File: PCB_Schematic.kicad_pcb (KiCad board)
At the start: 2 copper layers, 78.9 x 94.7 mm, 111 parts, among them J2 Programming Header, J3 SDOAG_Connector, J4 Power_Connector, J5 Ultrasonic, J6 USB_A, J7 IMU_1, J8 IMU_2, Q1 BSS138, SW1 Reset Switch, U1 STM32F091RCTx, U2 FT232RL, U3 LM1117MP-ADJ, U4 TPS54331QDRQ1, U5 MAX7375AXR805

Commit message: hi
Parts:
- moved H2 1.74 mm to (163.7, 36.1)
- moved H1 1.05 mm to (91.4, 36.1)
- moved H4 1.05 mm to (163.3, 124.0)
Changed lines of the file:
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@@
 	(footprint "MountingHole:MountingHole_2.2mm_M2"
 		(layer "F.Cu")
-		(at 91.694 37.084)
+		(at 91.44 36.068)
 		(descr "Mounting Hole 2.2mm, no annular, M2")
 		(tags "mounting hole 2.2mm no annular m2")
@@
 	(footprint "MountingHole:MountingHole_2.2mm_M2"
 		(layer "F.Cu")
-		(at 163.068 122.936)
+		(at 163.322 123.952)
 		(descr "Mounting Hole 2.2mm, no annular, M2")
 		(tags "mounting hole 2.2mm no annular m2")
@@
 	(footprint "MountingHole:MountingHole_2.2mm_M2"
 		(layer "F.Cu")
-		(at 162.56 37.338)
+		(at 163.749 36.068)
 		(descr "Mounting Hole 2.2mm, no annular, M2")
 		(tags "mounting hole 2.2mm no annular m2")

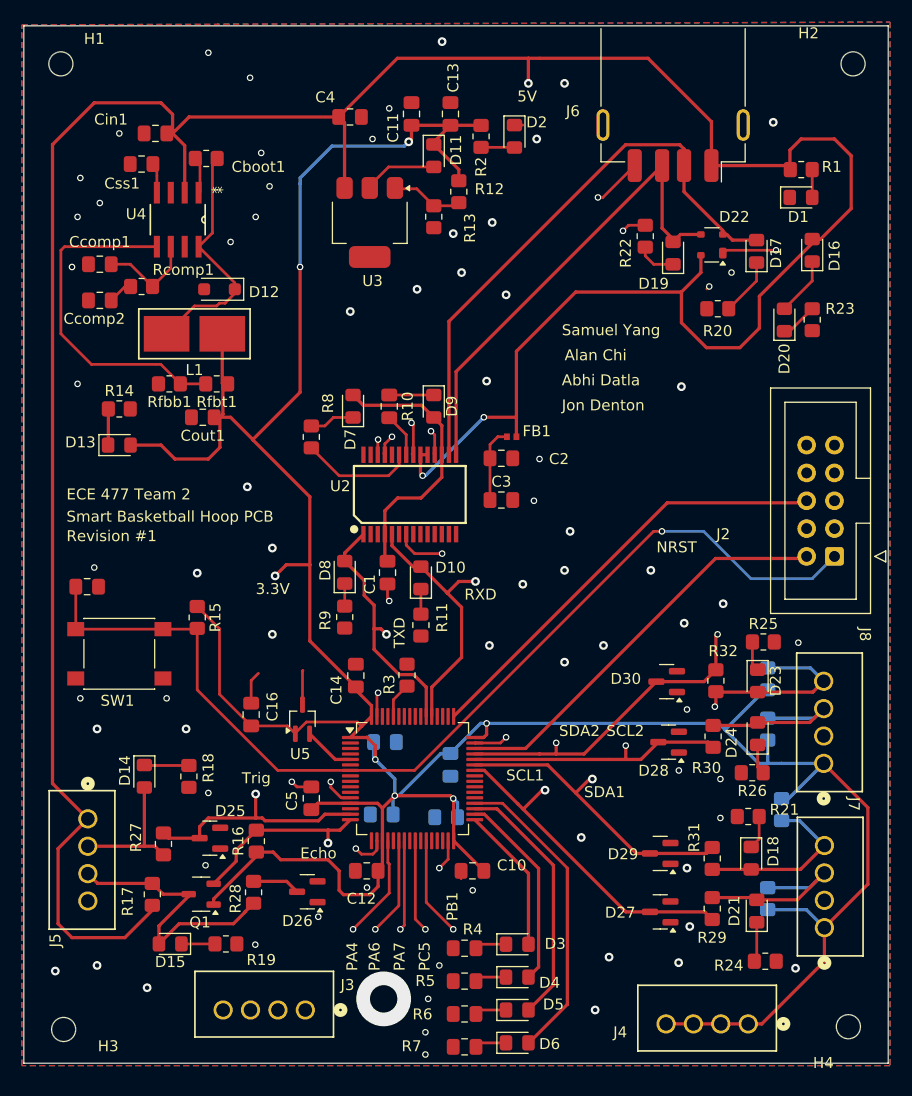
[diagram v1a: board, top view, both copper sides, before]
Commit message: mounting holes locations
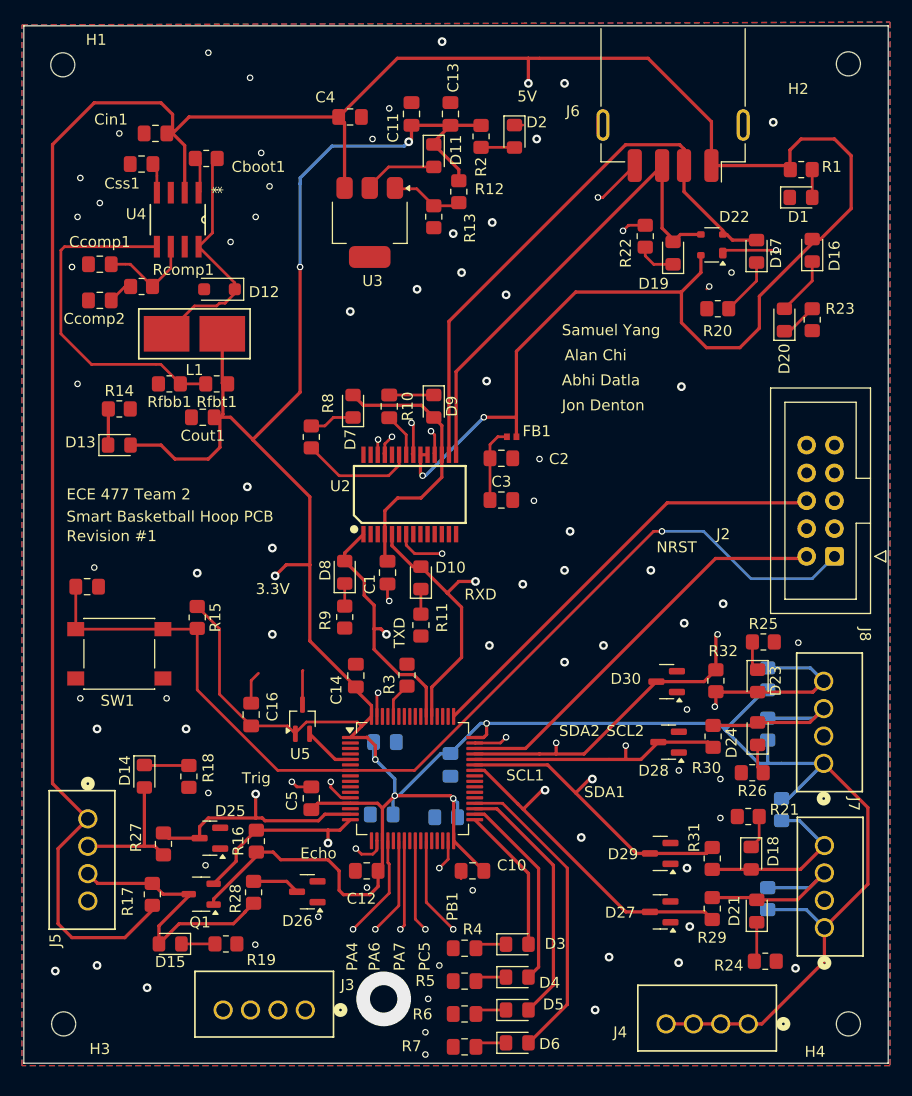
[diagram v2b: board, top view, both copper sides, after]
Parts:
- moved H3 0.51 mm to (91.7, 123.7)
- moved H2 0.43 mm to (163.3, 36.1)
- moved H4 0.25 mm to (163.3, 123.7)
- moved H1 0.19 mm to (91.6, 36.2)
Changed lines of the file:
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@@
 	(footprint "MountingHole:MountingHole_2.2mm_M2"
 		(layer "F.Cu")
-		(at 91.44 36.068)
+		(at 91.613 36.156)
 		(descr "Mounting Hole 2.2mm, no annular, M2")
 		(tags "mounting hole 2.2mm no annular m2")
@@
 	(footprint "MountingHole:MountingHole_2.2mm_M2"
 		(layer "F.Cu")
-		(at 163.322 123.952)
+		(at 163.322 123.698)
 		(descr "Mounting Hole 2.2mm, no annular, M2")
 		(tags "mounting hole 2.2mm no annular m2")
 		(property "Reference" "H4"
-			(at -2.286 3.302 0)
+			(at -3.048 2.54 0)
 			(layer "F.SilkS")
 			(effects
@@
 		)
 		(property "Value" "MountingHole"
-			(at -2.129 -3.744 0)
+			(at -1.524 -3.302 0)
 			(layer "F.Fab")
 			(effects
@@
 	(footprint "MountingHole:MountingHole_2.2mm_M2"
 		(layer "F.Cu")
-		(at 163.749 36.068)
+		(at 163.322 36.068)
 		(descr "Mounting Hole 2.2mm, no annular, M2")
 		(tags "mounting hole 2.2mm no annular m2")
 		(property "Reference" "H2"
-			(at -4.064 -2.794 180)
+			(at -4.572 2.286 180)
 			(layer "F.SilkS")
 			(effects
@@
 		)
 		(property "Value" "MountingHole"
-			(at -7.971 -0.95 0)
+			(at -2.286 3.556 0)
 			(layer "F.Fab")
 			(effects
@@
 	(footprint "MountingHole:MountingHole_2.2mm_M2"
 		(layer "F.Cu")
-		(at 91.694 124.206)
+		(at 91.694 123.698)
 		(descr "Mounting Hole 2.2mm, no annular, M2")
 		(tags "mounting hole 2.2mm no annular m2")
 		(property "Reference" "H3"
-			(at 4.064 1.524 0)
+			(at 3.302 2.286 0)
 			(layer "F.SilkS")
 			(effects

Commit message: updated fp
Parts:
- added D11: BAT60JFILM, Diode_SMD:D_SOD-323_HandSoldering, F.Cu at (125.7, 53.6)
- D12: footprint Diode_SMD:D_SOD-123F -> Diode_SMD:D_SOD-123
- D16: footprint Diode_SMD:D_0805_2012Metric_Pad1.15x1.40mm_HandSolder -> Diode_SMD:D_SOD-323_HandSoldering
- D22: footprint Package_TO_SOT_SMD:SOT-143 -> Library:PRT
- moved D12 12.5 mm to (109.7, 44.7), turned to 0 degrees
- moved D16 0.25 mm to (160.0, 53.3)
- turned D22 to 90 degrees
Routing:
- net +3.3V: track 301.1 -> 310.2 mm
- net Net-(D11-A): track 6.83 -> 15.1 mm
- net GND: track 53.6 -> 57.0 mm
- net Net-(D12-K): track 22.0 -> 24.3 mm

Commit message: BOM done
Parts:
- SW1: footprint Button_Switch_SMD:SW_SPST_PTS645 -> Library:SW_TS04-66-55-BK-160-SMT
- moved J2 0.36 mm to (161.8, 81.3)
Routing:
- net GND: track 57.0 -> 59.8 mm, vias 89 -> 91
- net /NRST: track 93.5 -> 91.2 mm
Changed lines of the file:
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@@
 	(footprint "Connector_IDC:IDC-Header_2x05_P2.54mm_Vertical"
 		(layer "F.Cu")
-		(at 162.052 81.026 180)
+		(at 161.798 81.28 180)
 		(descr "Through hole IDC box header, 2x05, 2.54mm pitch, DIN 41651 / IEC 60603-13, double rows, https://docs.google.com/spreadsheets/d/16SsEcesNF15N3Lb4niX7dcUr-NY5_MFPQhobNuNppn4/edit#gid=0")
 		(tags "Through hole vertical IDC box header THT 2x05 2.54mm double row")
 		(property "Reference" "J2"
-			(at 10.16 2.032 0)
+			(at 1.27 -6.1 360)
 			(layer "F.SilkS")
 			(effects
@@
 		)
 		(property "Value" "Programming Header"
-			(at 3.302 16.51 0)
+			(at 1.27 16.26 360)
 			(layer "F.Fab")
 			(effects
@@
 		)
 		(fp_text user "${REFERENCE}"
-			(at 10.16 13.212 90)
+			(at 1.27 5.08 90)
 			(layer "F.Fab")
 			(effects
@@
 		)
 	)
-	(footprint "Button_Switch_SMD:SW_SPST_PTS645"
+	(footprint "Library:SW_TS04-66-55-BK-160-SMT"
 		(layer "F.Cu")
 		(at 96.774 89.916 180)
-		(descr "C&K Components SPST SMD PTS645 Series 6mm Tact Switch")
-		(tags "SPST Button Switch")
 		(property "Reference" "SW1"
-			(at 0.17 -4.282 0)
+			(at -0.508 -4.318 180)
 			(layer "F.SilkS")
 			(effects
@@
 		)
 		(property "Value" "Reset Switch"
-			(at 0 4.15 0)
+			(at 10.922 3.81 180)
 			(layer "F.Fab")
 			(effects
@@
 			)
 		)
-		(property "Footprint" "Button_Switch_SMD:SW_SPST_PTS645"
+		(property "Footprint" "Library:SW_TS04-66-55-BK-160-SMT"
 			(at 0 0 180)
-			(unlocked yes)
 			(layer "F.Fab")
 			(hide yes)
@@
 		(property "Datasheet" ""
 			(at 0 0 180)
-			(unlocked yes)
 			(layer "F.Fab")
 			(hide yes)
@@
 		(property "Description" "Push button switch, generic, two pins"
 			(at 0 0 180)
-			(unlocked yes)
 			(layer "F.Fab")
 			(hide yes)
@@
 		(attr smd)
 		(fp_line
-			(start 3.23 3.23)
-			(end 3.23 3.2)
-			(stroke
-				(width 0.12)
-				(type solid)
-			)
-			(layer "F.SilkS")
-		)
-		(fp_line
-			(start 3.23 -1.3)
-			(end 3.23 1.3)
-			(stroke
-				(width 0.12)
-				(type solid)
-			)
-			(layer "F.SilkS")
-		)
-		(fp_line
-			(start 3.23 -3.23)
-			(end 3.23 -3.2)
-			(stroke
-				(width 0.12)
-				(type solid)
-			)
-			(layer "F.SilkS")
-		)
-		(fp_line
-			(start -3.23 3.23)
-			(end 3.23 3.23)
+			(start 3 3)
+			(end 3 -3)
 			(stroke
-				(width 0.12)
+				(width 0.127)
 				(type solid)
 			)
@@
 		)
 		(fp_line
-			(start -3.23 3.23)
-			(end -3.23 3.2)
+			(start 3 -3)
+			(end -3 -3)
 			(stroke
-				(width 0.12)
+				(width 0.127)
 				(type solid)
 			)
@@
 		)
 		(fp_line
-			(start -3.23 -1.3)
-			(end -3.23 1.3)
+			(start -3 3)
+			(end 3 3)
 			(stroke
-				(width 0.12)
+				(width 0.127)
 				(type solid)
 			)
@@
 		)
 		(fp_line
-			(start -3.23 -3.2)
-			(end -3.23 -3.23)
+			(start -3 -3)
+			(end -3 3)
 			(stroke
-				(width 0.12)
+				(width 0.127)
 				(type solid)
 			)
 			(layer "F.SilkS")
 		)
-		(fp_line
-			(start -3.23 -3.23)
-			(end 3.23 -3.23)
+		(fp_circle
+			(center -6.25 -2.25)
+			(end -6.15 -2.25)
 			(stroke
-				(width 0.12)
+				(width 0.2)
 				(type solid)
 			)
+			(fill none)
 			(layer "F.SilkS")
 		)
 		(fp_line
-			(start 5.05 3.4)
-			(end 5.05 -3.4)
+			(start 5.85 3.25)
+			(end 5.85 -3.25)
 			(stroke
 				(width 0.05)
@@
 		)
 		(fp_line
-			(start -5.05 3.4)
-			(end 5.05 3.4)
+			(start 5.85 -3.25)
+			(end -5.85 -3.25)
 			(stroke
 				(width 0.05)
@@
 		)
 		(fp_line
-			(start -5.05 -3.4)
-			(end 5.05 -3.4)
+			(start -5.85 3.25)
+			(end 5.85 3.25)
 			(stroke
 				(width 0.05)
@@
 		)
 		(fp_line
-			(start -5.05 -3.4)
-			(end -5.05 3.4)
+			(start -5.85 -3.25)
+			(end -5.85 3.25)
 			(stroke
 				(width 0.05)
@@
 			(end 3 -3)
 			(stroke
-				(width 0.1)
+				(width 0.127)
 				(type solid)
 			)
@@
 			(end -3 -3)
 			(stroke
-				(width 0.1)
+				(width 0.127)
 				(type solid)
 			)
@@
 			(end 3 3)
 			(stroke
-				(width 0.1)
+				(width 0.127)
 				(type solid)
 			)
@@
 			(end -3 3)
 			(stroke
-				(width 0.1)
+				(width 0.127)
 				(type solid)
 			)
@@
 		)
 		(fp_circle
-			(center 0 0)
-			(end 1.75 -0.05)
+			(center -6.25 -2.25)
+			(end -6.15 -2.25)
 			(stroke
-				(width 0.1)
+				(width 0.2)
 				(type solid)
 			)
@@
 			(layer "F.Fab")
 		)
-		(fp_text user "${REFERENCE}"
-			(at 0.17 -4.282 0)
-			(layer "F.Fab")
-			(effects
-				(font
-					(size 1 1)
-					(thickness 0.15)
-				)
-			)
-		)
-		(pad "1" smd rect
-			(at -3.98 -2.25 180)
-			(size 1.55 1.3)
-			(layers "F.Cu" "F.Paste" "F.Mask")
-			(net 1 "GND")
-			(pinfunction "1")
-			(pintype "passive")
-		)
 		(pad "1" smd rect
-			(at 3.98 -2.25 180)
-			(size 1.55 1.3)
+			(at -4.55 -2.25 180)
+			(size 2.1 1.4)
 			(layers "F.Cu" "F.Paste" "F.Mask")
 			(net 1 "GND")
 			(pinfunction "1")
 			(pintype "passive")
+			(solder_mask_margin 0.102)
 		)
 		(pad "2" smd rect
-			(at -3.98 2.25 180)
-			(size 1.55 1.3)
+			(at -4.55 2.25 180)
+			(size 2.1 1.4)
 			(layers "F.Cu" "F.Paste" "F.Mask")
 			(net 5 "/NRST")
 			(pinfunction "2")
 			(pintype "passive")
+			(solder_mask_margin 0.102)
 		)
-		(pad "2" smd rect
-			(at 3.98 2.25 180)
-			(size 1.55 1.3)
+		(pad "3" smd rect
+			(at 4.55 -2.25 180)
+			(size 2.1 1.4)
 			(layers "F.Cu" "F.Paste" "F.Mask")
-			(net 5 "/NRST")
-			(pinfunction "2")
-			(pintype "passive")
+			(solder_mask_margin 0.102)
 		)
-		(model "${KICAD8_3DMODEL_DIR}/Button_Switch_SMD.3dshapes/SW_SPST_PTS645.wrl"
-			(offset
-				(xyz 0 0 0)
-			)
-			(scale
-				(xyz 1 1 1)
-			)
-			(rotate
-				(xyz 0 0 0)
-			)
+		(pad "4" smd rect
+			(at 4.55 2.25 180)
+			(size 2.1 1.4)
+			(layers "F.Cu" "F.Paste" "F.Mask")
+			(solder_mask_margin 0.102)
 		)
 	)
@@
 	)
 	(segment
+		(start 101.324 94.256)
+		(end 100.838 94.742)
+		(width 0.254)
+		(layer "F.Cu")
+		(net 1)
+	)
+	(segment
 		(start 126.791 108.667)
 		(end 125.984 109.474)
@@
 	)
 	(segment
+		(start 101.324 92.166)
+		(end 101.324 94.256)
+		(width 0.254)
+		(layer "F.Cu")
+		(net 1)
+	)
+	(segment
 		(start 129.272 98.058)
 		(end 129.286 98.044)
@@
 	)
 	(via
+		(at 100.838 94.742)
+		(size 0.6)
+		(drill 0.381)
+		(layers "F.Cu" "B.Cu")
+		(net 1)
+	)
+	(via
 		(at 104.902 102.616)
 		(size 0.6)
@@
 	)
 	(via
+		(at 113.538 91.44)
+		(size 0.6)
+		(drill 0.381)
+		(layers "F.Cu" "B.Cu")
+		(net 1)
+	)
+	(via
 		(at 110.744 88.138)
 		(size 0.8)
@@
 	)
 	(via
-		(at 101.092 93.98)
+		(at 109.474 91.694)
 		(size 0.6)
 		(drill 0.381)
@@
 	)
 	(via
-		(at 93.218 93.98)
+		(at 97.028 95.758)
 		(size 0.6)
 		(drill 0.381)
@@
 	)
 	(segment
-		(start 92.801 87.659)
-		(end 92.794 87.666)
-		(width 0.25)
+		(start 96.678 87.666)
+		(end 101.324 87.666)
+		(width 0.254)
 		(layer "F.Cu")
 		(net 5)
@@
 	)
 	(segment
-		(start 103.818 87.666)
-		(end 103.886 87.598)
-		(width 0.25)
+		(start 92.801 83.789)
+		(end 96.678 87.666)
+		(width 0.254)
 		(layer "F.Cu")
 		(net 5)
 	)
 	(segment
-		(start 92.801 83.789)
-		(end 92.801 87.659)
+		(start 103.818 87.666)
+		(end 103.886 87.598)
 		(width 0.254)
 		(layer "F.Cu")
@@
 	)
 	(segment
-		(start 92.794 87.666)
-		(end 100.754 87.666)
-		(width 0.254)
-		(layer "F.Cu")
-		(net 5)
-	)
-	(segment
 		(start 123.724 100.558)
 		(end 117.866 100.558)
@@
 	)
 	(segment
-		(start 100.754 87.666)
+		(start 101.324 87.666)
 		(end 103.818 87.666)
 		(width 0.254)

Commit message: footprint verf
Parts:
- D11: footprint Diode_SMD:D_0805_2012Metric_Pad1.15x1.40mm_HandSolder -> Diode_SMD:D_SOD-323_HandSoldering
- moved D11 0.55 mm to (125.2, 44.9)
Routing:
- net +3.3V: track 310.2 -> 310.8 mm
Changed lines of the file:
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@@
 		(tags "Through hole vertical IDC box header THT 2x05 2.54mm double row")
 		(property "Reference" "J2"
-			(at 1.27 -6.1 360)
+			(at 1.27 -6.1 0)
 			(layer "F.SilkS")
 			(effects
@@
 		)
 		(property "Value" "Programming Header"
-			(at 1.27 16.26 360)
+			(at 1.27 16.26 0)
 			(layer "F.Fab")
 			(effects
@@
 		)
 		(property "Value" "Reset Switch"
-			(at 10.922 3.81 180)
+			(at -0.508 0.762 180)
 			(layer "F.Fab")
 			(effects
@@
 		)
 	)
-	(footprint "Diode_SMD:D_0805_2012Metric_Pad1.15x1.40mm_HandSolder"
+	(footprint "Diode_SMD:D_SOD-323_HandSoldering"
 		(layer "F.Cu")
-		(at 125.476 44.45 -90)
-		(descr "Diode SMD 0805 (2012 Metric), square (rectangular) end terminal, IPC_7351 nominal, (Body size source: https://docs.google.com/spreadsheets/d/1BsfQQcO9C6DZCsRaXUlFlo91Tg2WpOkGARC1WS5S8t0/edit?usp=sharing), generated with kicad-footprint-generator")
-		(tags "diode handsolder")
+		(at 125.222 44.938 -90)
+		(descr "SOD-323")
+		(tags "SOD-323")
 		(property "Reference" "D11"
-			(at -0.508 -2.032 90)
+			(at -0.742 -2.286 -90)
 			(layer "F.SilkS")
 			(effects
@@
 		)
 		(property "Value" "BAT60JFILM"
-			(at 2 1.142 90)
+			(at 0.1 1.9 -90)
 			(layer "F.Fab")
 			(effects
@@
 			)
 		)
-		(property "Footprint" "Diode_SMD:D_0805_2012Metric_Pad1.15x1.40mm_HandSolder"
+		(property "Footprint" "Diode_SMD:D_SOD-323_HandSoldering"
 			(at 0 0 -90)
 			(unlocked yes)
@@
 		(attr smd)
 		(fp_line
-			(start -1.86 0.96)
-			(end 1 0.96)
+			(start -2.01 0.85)
+			(end 1.25 0.85)
 			(stroke
 				(width 0.12)
@@
 		)
 		(fp_line
-			(start -1.86 -0.96)
-			(end -1.86 0.96)
+			(start -2.01 -0.85)
+			(end -2.01 0.85)
 			(stroke
 				(width 0.12)
@@
 		)
 		(fp_line
-			(start 1 -0.96)
-			(end -1.86 -0.96)
+			(start -2.01 -0.85)
+			(end 1.25 -0.85)
 			(stroke
 				(width 0.12)
@@
 		)
 		(fp_line
-			(start -1.85 0.95)
-			(end -1.85 -0.95)
+			(start -2 0.95)
+			(end 2 0.95)
 			(stroke
 				(width 0.05)
@@
 		)
 		(fp_line
-			(start 1.85 0.95)
-			(end -1.85 0.95)
+			(start -2 -0.95)
+			(end -2 0.95)
 			(stroke
 				(width 0.05)
@@
 		)
 		(fp_line
-			(start -1.85 -0.95)
-			(end 1.85 -0.95)
+			(start -2 -0.95)
+			(end 2 -0.95)
 			(stroke
 				(width 0.05)
@@
 		)
 		(fp_line
-			(start 1.85 -0.95)
-			(end 1.85 0.95)
+			(start 2 -0.95)
+			(end 2 0.95)
 			(stroke
 				(width 0.05)
@@
 		)
 		(fp_line
-			(start -1 0.6)
-			(end 1 0.6)
+			(start -0.9 0.7)
+			(end -0.9 -0.7)
 			(stroke
 				(width 0.1)
@@
 		)
 		(fp_line
-			(start 1 0.6)
-			(end 1 -0.6)
+			(start 0.9 0.7)
+			(end -0.9 0.7)
 			(stroke
 				(width 0.1)
@@
 		)
 		(fp_line
-			(start -1 -0.3)
-			(end -1 0.6)
+			(start 0.2 0.35)
+			(end -0.3 0)
 			(stroke
 				(width 0.1)
@@
 		)
 		(fp_line
-			(start -0.7 -0.6)
-			(end -1 -0.3)
+			(start -0.3 0)
+			(end -0.5 0)
 			(stroke
 				(width 0.1)
@@
 		)
 		(fp_line
-			(start 1 -0.6)
-			(end -0.7 -0.6)
+			(start -0.3 0)
+			(end 0.2 -0.35)
+			(stroke
+				(width 0.1)
+				(type solid)
+			)
+			(layer "F.Fab")
+		)
+		(fp_line
+			(start 0.2 0)
+			(end 0.45 0)
+			(stroke
+				(width 0.1)
+				(type solid)
+			)
+			(layer "F.Fab")
+		)
+		(fp_line
+			(start -0.3 -0.35)
+			(end -0.3 0.35)
+			(stroke
+				(width 0.1)
+				(type solid)
+			)
+			(layer "F.Fab")
+		)
+		(fp_line
+			(start 0.2 -0.35)
+			(end 0.2 0.35)
+			(stroke
+				(width 0.1)
+				(type solid)
+			)
+			(layer "F.Fab")
+		)
+		(fp_line
+			(start -0.9 -0.7)
+			(end 0.9 -0.7)
+			(stroke
+				(width 0.1)
+				(type solid)
+			)
+			(layer "F.Fab")
+		)
+		(fp_line
+			(start 0.9 -0.7)
+			(end 0.9 0.7)
 			(stroke
 				(width 0.1)
@@
 		)
 		(fp_text user "${REFERENCE}"
-			(at 0 0 90)
+			(at 0 -1.85 -90)
 			(layer "F.Fab")
 			(effects
 				(font
-					(size 0.5 0.5)
-					(thickness 0.08)
+					(size 1 1)
+					(thickness 0.15)
 				)
 			)
 		)
 		(pad "1" smd roundrect
-			(at -1.025 0 270)
-			(size 1.15 1.4)
+			(at -1.25 0 270)
+			(size 1 1)
 			(layers "F.Cu" "F.Paste" "F.Mask")
-			(roundrect_rratio 0.217391)
+			(roundrect_rratio 0.25)
 			(net 4 "+3.3V")
 			(pinfunction "K")
@@
 		)
 		(pad "2" smd roundrect
-			(at 1.025 0 270)
-			(size 1.15 1.4)
+			(at 1.25 0 270)
+			(size 1 1)
 			(layers "F.Cu" "F.Paste" "F.Mask")
-			(roundrect_rratio 0.217391)
+			(roundrect_rratio 0.25)
 			(net 28 "Net-(D11-A)")
 			(pinfunction "A")
 			(pintype "passive")
 		)
-		(model "${KICAD8_3DMODEL_DIR}/Diode_SMD.3dshapes/D_0805_2012Metric.wrl"
+		(model "${KICAD8_3DMODEL_DIR}/Diode_SMD.3dshapes/D_SOD-323.wrl"
 			(offset
 				(xyz 0 0 0)
@@
 	)
 	(segment
+		(start 127 41.91)
+		(end 127 41.6775)
+		(width 0.25)
+		(layer "F.Cu")
+		(net 4)
+	)
+	(segment
 		(start 119.38 97.536)
 		(end 120.142 98.298)
@@
 	)
 	(segment
-		(start 125.476 43.425)
-		(end 125.476 43.2015)
-		(width 0.3)
-		(layer "F.Cu")
-		(net 4)
-	)
-	(segment
 		(start 120.396 109.728)
 		(end 120.396 111.155239)
@@
 	)
 	(segment
+		(start 125.222 43.688)
+		(end 127 41.91)
+		(width 0.25)
+		(layer "F.Cu")
+		(net 4)
+	)
+	(segment
 		(start 115.824 108.712)
 		(end 111.506 108.712)
@@
 	)
 	(segment
-		(start 125.476 43.425)
-		(end 127.762 45.711)
-		(width 0.3)
-		(layer "F.Cu")
-		(net 4)
-	)
-	(segment
 		(start 106.934 68.326)
 		(end 108.9494 70.3414)
@@
 	)
 	(segment
-		(start 125.476 43.2015)
-		(end 127 41.6775)
-		(width 0.3)
+		(start 125.222 43.688)
+		(end 125.739 43.688)
+		(width 0.25)
 		(layer "F.Cu")
 		(net 4)
@@
 	)
 	(segment
+		(start 125.739 43.688)
+		(end 127.762 45.711)
+		(width 0.25)
+		(layer "F.Cu")
+		(net 4)
+	)
+	(segment
 		(start 160.879 115.17)
 		(end 161.133 114.916)
@@
 	)
 	(segment
-		(start 121.355 45.475)
-		(end 125.476 45.475)
-		(width 0.254)
+		(start 125.222 46.188)
+		(end 125.105 46.071)
+		(width 0.25)
 		(layer "F.Cu")
 		(net 28)
@@
 	)
 	(segment
-		(start 119.634 47.196)
-		(end 121.355 45.475)
-		(width 0.254)
+		(start 120.959 46.071)
+		(end 119.634 47.396)
+		(width 0.25)
 		(layer "F.Cu")
 		(net 28)
@@
 		(layer "F.Cu")
 		(net 28)
+	)
+	(segment
+		(start 125.105 46.071)
+		(end 120.959 46.071)
+		(width 0.25)
+		(layer "F.Cu")
+		(net 28)

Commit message: new FB
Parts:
- moved C2 1.22 mm to (131.8, 73.3)
- moved C3 1.22 mm to (131.8, 77.1)
- moved FB1 0.57 mm to (132.3, 70.6)
- renumbered D12 to D10, D13 to D11, D16 to D12, D20 to D13, D22 to D14, D25 to D15, D26 to D16, D27 to D17, D28 to D18, D29 to D19, D30 to D20, D9 to D8, D11 to D9, J2 to J1, J3 to J2, J4 to J3, J5 to J4, J6 to J5, J7 to J6, J8 to J7, R12 to R10, R13 to R11, R14 to R12, R15 to R13, R16 to R14, R17 to R15, R34 to R16, R23 to R17, R33 to R18, R35 to R19, R36 to R20, R27 to R21, R28 to R22, R29 to R23, R30 to R24, R31 to R25, R32 to R26, R10 to R9
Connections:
- Cboot1 pad 1: Net-(D12-K) (its old number) -> Net-(D10-K)
- D10 pad 1: Net-(D12-K) (its old number) -> Net-(D10-K)
- D8 pad 1: Net-(D9-K) -> Net-(D8-K)
- L1 pad 1: Net-(D12-K) (its old number) -> Net-(D10-K)
- R9 pad 1: Net-(D9-K) -> Net-(D8-K)
- U4 pad 8: Net-(D12-K) (its old number) -> Net-(D10-K)
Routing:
- net Net-(D10-K): track 2.29 -> 69.3 mm, vias 0 -> 2
- net Net-(D8-K): track 2.06 -> 35.3 mm
- net Net-(D12-K) (its old number): track 24.3 -> 0.00 mm
- net GND: track 59.8 -> 64.1 mm
- net Net-(D9-K): track 4.06 -> 0.00 mm
- net +5V: track 263.0 -> 263.6 mm

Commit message: updates
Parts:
- removed the D10 at (124.3, 83.0)
- removed the D8 at (117.3, 82.5)
- removed the D9 at (125.2, 44.9)
- removed the R11 at (124.3, 87.3)
- removed the R9 at (117.3, 86.6)
- moved U3 0.15 mm to (119.6, 50.7)
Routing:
- net Net-(D10-K): track 69.3 -> 24.3 mm, vias 2 -> 0
- net Net-(D8-K): track 35.3 -> 4.06 mm
- net Net-(D9-A): track 14.8 -> 8.57 mm
- net +5V: track 263.6 -> 266.5 mm
- net GND: track 64.1 -> 66.4 mm, vias 91 -> 92
- net +3.3V: track 310.8 -> 309.0 mm
- net /RXD: track 23.8 -> 22.4 mm
